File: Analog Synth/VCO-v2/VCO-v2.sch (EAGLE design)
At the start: 64 parts, among them IC1 TL084P, IC2 TL084P, IC3 78L09, IC5 79L09\, Q1 J310, Q2 J310, T1 2N3904, T2 2N3904, T3 2N3904, T4 2N3904, T7 2N3904, U1 CA3096

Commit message: VCO-v2 PWM and Triangle outputs
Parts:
- removed CV_MANUAL: 10k, pot:TRIM_US-B64Y
- removed CV_MANUAL1, CV_MANUAL2: 100k log, pot:TRIM_US-B64Y
- added ATTN_CV_B, ATTN_CV_C: 100k log, pot:TRIM_US-B64Y
- added C10, C9: 100u, rcl:CPOL-USE3.5-10
- added C11, C13, C16, C17: 10u, rcl:CPOL-USE3.5-10
- added C12, C14, C15, C18, C19, C20, C21: 0.1u, resistor:C-EU025-050X050
- added CV-PWM, PWM, TRIANGLE: I/O, !synth_sch:MONO_JACK
- added FREQ-MAN: 10k lin, pot:TRIM_US-B64Y
- added IC7: TL084P, linear:TL084P
- added PWM-MAN: 100k lin, pot:TRIM_US-B64Y
- added R30, R31: 10k, resistor:R-US_0204/7
- added R32, R35, R36: 2.2k, resistor:R-US_0204/7
- added R33, R34, R38: 100k, resistor:R-US_0204/7
- added R37: 47k, resistor:R-US_0204/7
- C8: value 100p -> 0.1u
- IC4: value (none) -> 78L05
- IC6: value (none) -> 79L05
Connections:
- new net N$27: IC2C.-IN, R30.2, R31.2
- new net N$28: R32.1, TRIANGLE.P2
- new net N$36: C21.1
- new net N$37: IC2D.OUT, R35.1
- new net N$38: PWM.P2, R35.2, R36.2
- new net N$39: IC7B.+IN, R37.2
- new net N$40: IC7B.-IN, IC7B.OUT, R34.1
- new net N$41: CV-PWM.P2, R37.1
- new net N$43: IC7A.-IN, R33.2, R34.2, R38.1
- new net N$44: IC2D.-IN, IC7A.OUT, R38.2
- new net N$45: PWM-MAN.S, R33.1
- new net TRIANGLE: IC2C.OUT, IC2D.+IN, R31.1, R32.2
- net +12V: now also C14.1, C8.1, C9.+, IC1P.V+, IC2P.V+
- net +5V: now also C17.+, C19.1, FREQ-MAN.A, PWM-MAN.A; no longer CV_MANUAL.A
- net +9V: now also C11.+, C18.1
- net -12V: now also C10.+, C12.1, C15.1, IC1P.V-, IC2P.V-
- net -5V: now also C16.+, FREQ-MAN.E, PWM-MAN.E; no longer CV_MANUAL.E
- net -9V: now also C13.+, C20.1
- net GND: now also ATTN_CV_B.A, ATTN_CV_C.A, C10.-, C11.-, C12.2, C13.-, C14.2, C15.2, C16.-, C17.-, C18.2, C19.2, C20.2, C21.2, C8.2, C9.-, CV-PWM.P$1, CV-PWM.P3, IC5.GND, IC7A.+IN, PWM.P$1, R30.1, R36.1, TRIANGLE.P$1; no longer CV_MANUAL1.A, CV_MANUAL2.A
- net N$1: now also FREQ-MAN.S; no longer CV_MANUAL.S
- net N$4: now also ATTN_CV_C.S; no longer CV_MANUAL2.S
- net N$6: now also ATTN_CV_B.S; no longer CV_MANUAL1.S
- net N$8: now also ATTN_CV_B.E; no longer CV_MANUAL1.E
- net N$9: now also ATTN_CV_C.E; no longer CV_MANUAL2.E
- net V-CAP-BUFF: now also IC2C.+IN
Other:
- note added: "IC1 power"
- note added: "IC2 power"

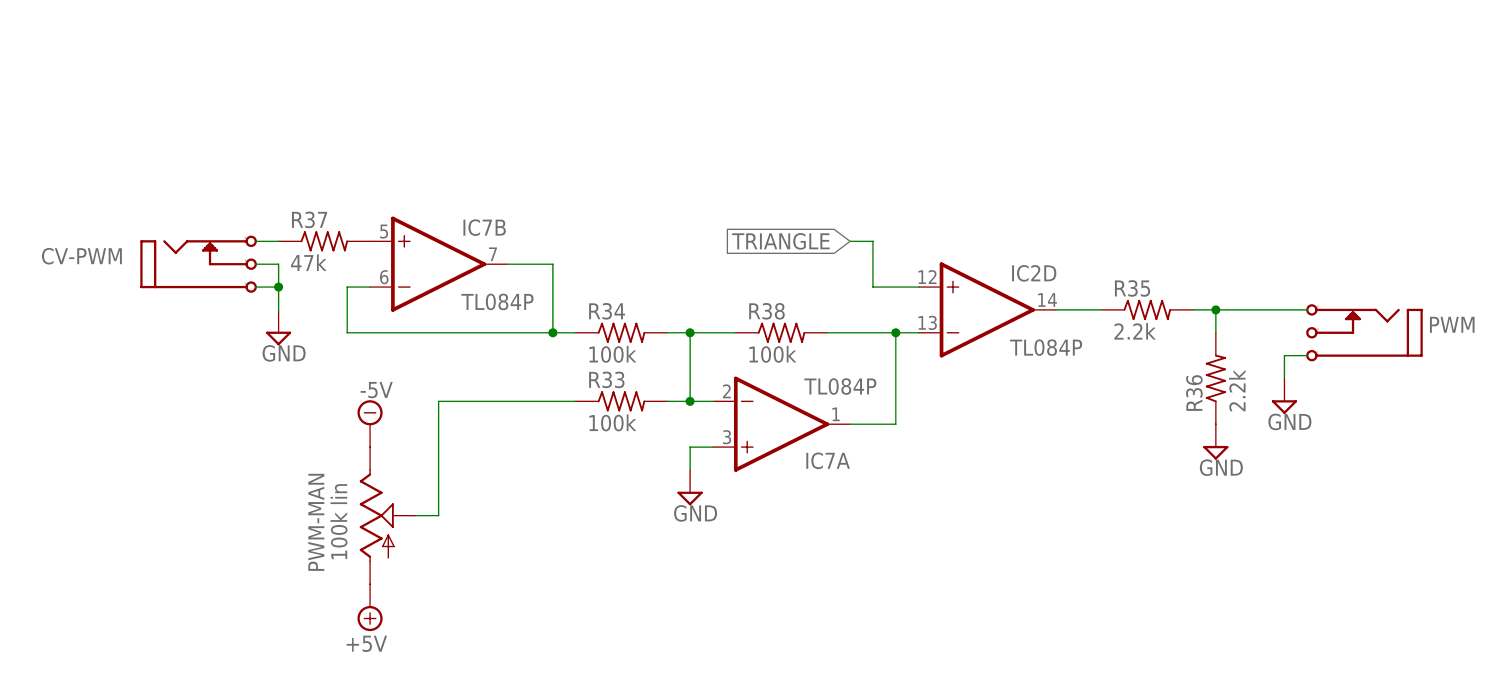
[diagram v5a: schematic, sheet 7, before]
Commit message: VCO-v2 PWM control voltage attenuation
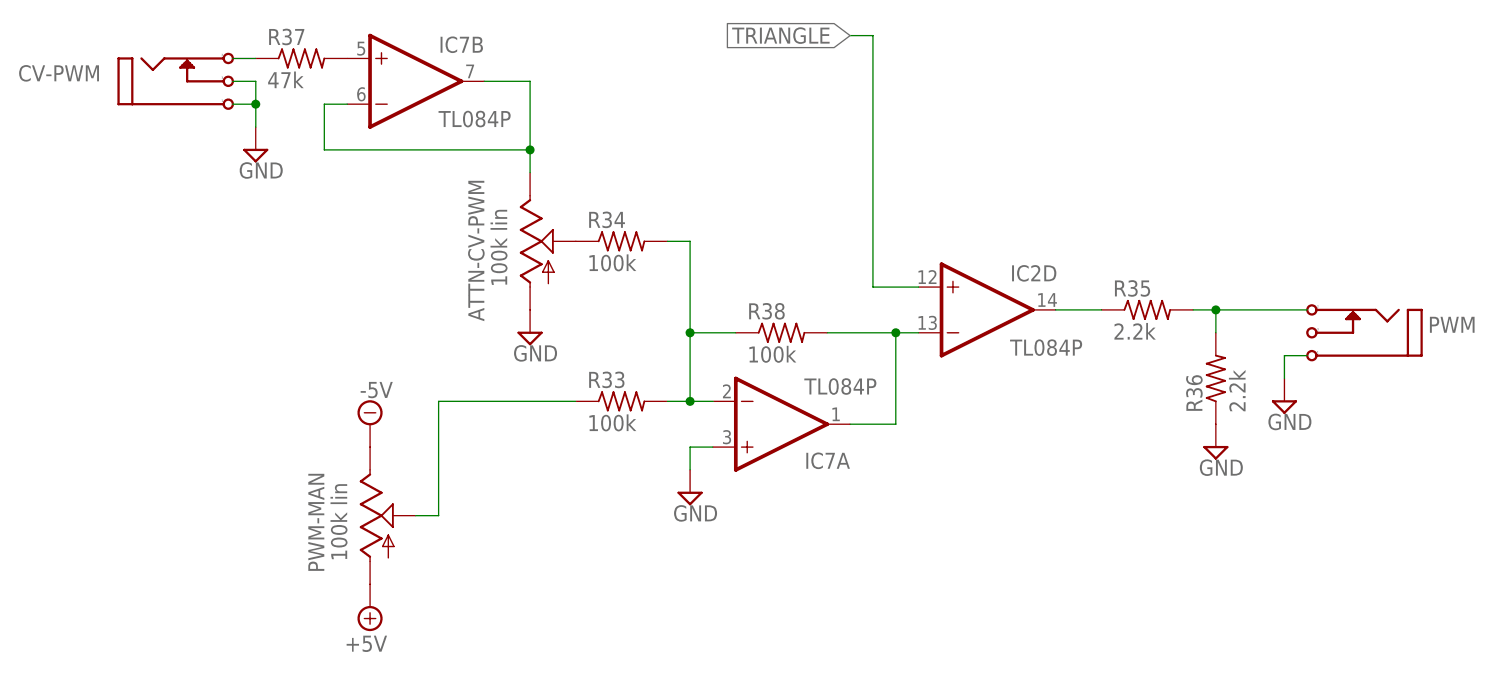
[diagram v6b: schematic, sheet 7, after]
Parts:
- added ATTN-CV-PWM: 100k lin, pot:TRIM_US-B64Y
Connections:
- new net N$42: ATTN-CV-PWM.S, R34.1
- net GND: now also ATTN-CV-PWM.A
- net N$40: now also ATTN-CV-PWM.E; no longer R34.1
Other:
- moved on the sheet: CV-PWM, IC7B, R34, R37
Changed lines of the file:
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@@
 <part name="PWM" library="!synth_sch" deviceset="MONO_JACK" device="" value="I/O"/>
 <part name="SUPPLY36" library="supply2" deviceset="GND" device=""/>
+<part name="ATTN-CV-PWM" library="pot" deviceset="TRIM_US-" device="B64Y" value="100k lin"/>
+<part name="SUPPLY39" library="supply2" deviceset="GND" device=""/>
 </parts>
 <sheets>
@@
 </plain>
 <instances>
-<instance part="IC7" gate="B" x="7.62" y="53.34"/>
+<instance part="IC7" gate="B" x="5.08" y="73.66"/>
 <instance part="IC7" gate="A" x="45.72" y="35.56" rot="MR180"/>
 <instance part="IC2" gate="D" x="68.58" y="48.26"/>
 <instance part="R33" gate="G$1" x="27.94" y="38.1"/>
-<instance part="R34" gate="G$1" x="27.94" y="45.72"/>
+<instance part="R34" gate="G$1" x="27.94" y="55.88"/>
 <instance part="R35" gate="G$1" x="86.36" y="48.26"/>
 <instance part="R36" gate="G$1" x="93.98" y="40.64" rot="R90"/>
 <instance part="SUPPLY40" gate="GND" x="93.98" y="33.02"/>
-<instance part="R37" gate="G$1" x="-5.08" y="55.88"/>
-<instance part="CV-PWM" gate="J1" x="-20.32" y="53.34" smashed="yes">
-<attribute name="NAME" x="-36.576" y="53.34" size="1.778" layer="96"/>
-</instance>
-<instance part="SUPPLY41" gate="GND" x="-10.16" y="45.72"/>
+<instance part="R37" gate="G$1" x="-7.62" y="76.2"/>
+<instance part="CV-PWM" gate="J1" x="-22.86" y="73.66" smashed="yes">
+<attribute name="NAME" x="-39.116" y="73.66" size="1.778" layer="96"/>
+</instance>
+<instance part="SUPPLY41" gate="GND" x="-12.7" y="66.04"/>
 <instance part="R38" gate="G$1" x="45.72" y="45.72"/>
 <instance part="SUPPLY42" gate="+5V" x="0" y="15.24" rot="R180"/>
@@
 </instance>
 <instance part="SUPPLY36" gate="GND" x="101.6" y="38.1"/>
+<instance part="ATTN-CV-PWM" gate="G$1" x="17.78" y="55.88" smashed="yes">
+<attribute name="NAME" x="12.7" y="46.99" size="1.778" layer="95" rot="R90"/>
+<attribute name="VALUE" x="15.24" y="50.8" size="1.778" layer="96" rot="R90"/>
+</instance>
+<instance part="SUPPLY39" gate="GND" x="17.78" y="45.72"/>
 </instances>
 <busses>
@@
 <segment>
 <pinref part="CV-PWM" gate="J1" pin="P3"/>
-<wire x1="-12.7" y1="53.34" x2="-10.16" y2="53.34" width="0.1524" layer="91"/>
-<wire x1="-10.16" y1="53.34" x2="-10.16" y2="50.8" width="0.1524" layer="91"/>
+<wire x1="-15.24" y1="73.66" x2="-12.7" y2="73.66" width="0.1524" layer="91"/>
+<wire x1="-12.7" y1="73.66" x2="-12.7" y2="71.12" width="0.1524" layer="91"/>
 <pinref part="CV-PWM" gate="J1" pin="P$1"/>
-<wire x1="-10.16" y1="50.8" x2="-12.7" y2="50.8" width="0.1524" layer="91"/>
-<wire x1="-10.16" y1="50.8" x2="-10.16" y2="48.26" width="0.1524" layer="91"/>
-<junction x="-10.16" y="50.8"/>
+<wire x1="-12.7" y1="71.12" x2="-15.24" y2="71.12" width="0.1524" layer="91"/>
+<wire x1="-12.7" y1="71.12" x2="-12.7" y2="68.58" width="0.1524" layer="91"/>
+<junction x="-12.7" y="71.12"/>
 <pinref part="SUPPLY41" gate="GND" pin="GND"/>
 </segment>
@@
 <wire x1="101.6" y1="43.18" x2="104.14" y2="43.18" width="0.1524" layer="91"/>
 </segment>
+<segment>
+<pinref part="ATTN-CV-PWM" gate="G$1" pin="A"/>
+<pinref part="SUPPLY39" gate="GND" pin="GND"/>
+</segment>
 </net>
 <net name="TRIANGLE" class="0">
@@
 <pinref part="IC2" gate="D" pin="+IN"/>
 <wire x1="60.96" y1="50.8" x2="55.88" y2="50.8" width="0.1524" layer="91"/>
-<wire x1="55.88" y1="50.8" x2="55.88" y2="55.88" width="0.1524" layer="91"/>
-<wire x1="55.88" y1="55.88" x2="53.34" y2="55.88" width="0.1524" layer="91"/>
-<label x="53.34" y="55.88" size="1.778" layer="95" rot="R180" xref="yes"/>
+<wire x1="55.88" y1="50.8" x2="55.88" y2="78.74" width="0.1524" layer="91"/>
+<wire x1="55.88" y1="78.74" x2="53.34" y2="78.74" width="0.1524" layer="91"/>
+<label x="53.34" y="78.74" size="1.778" layer="95" rot="R180" xref="yes"/>
 </segment>
 </net>
@@
 <segment>
 <pinref part="IC7" gate="B" pin="-IN"/>
-<wire x1="0" y1="50.8" x2="-2.54" y2="50.8" width="0.1524" layer="91"/>
-<wire x1="-2.54" y1="50.8" x2="-2.54" y2="45.72" width="0.1524" layer="91"/>
-<wire x1="-2.54" y1="45.72" x2="20.32" y2="45.72" width="0.1524" layer="91"/>
-<wire x1="20.32" y1="45.72" x2="20.32" y2="53.34" width="0.1524" layer="91"/>
+<wire x1="-2.54" y1="71.12" x2="-5.08" y2="71.12" width="0.1524" layer="91"/>
+<wire x1="-5.08" y1="71.12" x2="-5.08" y2="66.04" width="0.1524" layer="91"/>
+<wire x1="-5.08" y1="66.04" x2="17.78" y2="66.04" width="0.1524" layer="91"/>
+<wire x1="17.78" y1="66.04" x2="17.78" y2="73.66" width="0.1524" layer="91"/>
 <pinref part="IC7" gate="B" pin="OUT"/>
-<wire x1="20.32" y1="53.34" x2="15.24" y2="53.34" width="0.1524" layer="91"/>
-<pinref part="R34" gate="G$1" pin="1"/>
-<wire x1="22.86" y1="45.72" x2="20.32" y2="45.72" width="0.1524" layer="91"/>
-<junction x="20.32" y="45.72"/>
+<wire x1="17.78" y1="73.66" x2="12.7" y2="73.66" width="0.1524" layer="91"/>
+<pinref part="ATTN-CV-PWM" gate="G$1" pin="E"/>
+<wire x1="17.78" y1="63.5" x2="17.78" y2="66.04" width="0.1524" layer="91"/>
+<junction x="17.78" y="66.04"/>
 </segment>
 </net>
@@
 <segment>
 <pinref part="R37" gate="G$1" pin="1"/>
-<wire x1="-10.16" y1="55.88" x2="-12.7" y2="55.88" width="0.1524" layer="91"/>
+<wire x1="-12.7" y1="76.2" x2="-15.24" y2="76.2" width="0.1524" layer="91"/>
 <pinref part="CV-PWM" gate="J1" pin="P2"/>
 </segment>
@@
 <wire x1="35.56" y1="38.1" x2="35.56" y2="45.72" width="0.1524" layer="91"/>
 <pinref part="R34" gate="G$1" pin="2"/>
-<wire x1="33.02" y1="45.72" x2="35.56" y2="45.72" width="0.1524" layer="91"/>
+<wire x1="33.02" y1="55.88" x2="35.56" y2="55.88" width="0.1524" layer="91"/>
+<wire x1="35.56" y1="55.88" x2="35.56" y2="45.72" width="0.1524" layer="91"/>
 <junction x="35.56" y="45.72"/>
 <pinref part="IC7" gate="A" pin="-IN"/>
@@
 </segment>
 </net>
+<net name="N$42" class="0">
+<segment>
+<pinref part="R34" gate="G$1" pin="1"/>
+<pinref part="ATTN-CV-PWM" gate="G$1" pin="S"/>
+</segment>
+</net>

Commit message: VCO-v2 Sine (from VCO-v1 basically)
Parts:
- added Q3, Q4: 2N3904, transistor-npn:2N3904
- added R-SINE-AMPL, R-SINE-ROUND: 100k lin, pot:TRIM_US-B64Y
- added R-SINE-SYMM: 10 kΩ, pot:TRIM_US-B64Y
- added R39, R40: 2.2 kΩ, resistor:R-US_0204/7
- added R41: 390 Ω, resistor:R-US_0204/7
- added R42: 18 kΩ, resistor:R-US_0204/7
- added R43, R44, R45, R46: 10 kΩ, resistor:R-US_0204/7
- added R47: 1k, resistor:R-US_0204/7
- added SINE: I/O, !synth_sch:MONO_JACK
- R32: value 2.2k -> 1k
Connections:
- net N$37 renamed PWM
- new net N$37: Q3.B, R-SINE-ROUND.E, R39.1
- new net N$46: Q4.B, R40.1
- new net N$47: Q3.E, R-SINE-SYMM.A, R41.1
- new net N$48: Q4.E, R-SINE-SYMM.E, R41.2
- new net N$49: R-SINE-SYMM.S, R42.1
- new net N$50: IC7C.-IN, Q3.C, R43.1, R46.1
- new net N$51: IC7C.OUT, R-SINE-AMPL.A, R46.2
- new net N$52: IC7C.+IN, Q4.C, R44.1, R45.2
- new net N$54: IC7D.-IN, R-SINE-AMPL.S
- new net N$55: R47.2, SINE.P2
- new net SINE: IC7D.OUT, R-SINE-AMPL.E, R47.1
- net +9V: now also R43.2, R44.2
- net -9V: now also R42.2
- net GND: now also IC7D.+IN, R39.2, R40.2, R45.1, SINE.P$1
- net TRIANGLE: now also R-SINE-ROUND.A, R-SINE-ROUND.S
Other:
- note added: "Triangle to Sine converter is a modified version of Thomas Henry's design."

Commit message: VCO-v2 LEDs sheet and signal names
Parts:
- added LED-CV-A, LED-CV-B, LED-CV-PWM, LED-PWM, LED-SINE, LED-TRIANGLE, LED_CV-C: (no value), led:LED3MM
- added R48, R49, R50, R51, R53, R54, R56: 4.7 kΩ, resistor:R-US_0204/7
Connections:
- removed net N$11: IC1C.-IN, IC1C.OUT, R6.1
- removed net N$5: IC1B.-IN, IC1B.OUT, R5.1
- removed net N$7: IC1A.-IN, IC1A.OUT, R4.1
- new net CV-A: IC1A.-IN, IC1A.OUT, LED-CV-A.A, R4.1
- new net CV-B: IC1B.-IN, IC1B.OUT, LED-CV-B.A, R5.1
- new net CV-C: IC1C.-IN, IC1C.OUT, LED_CV-C.A, R6.1
- new net CV-PWM: IC2D.-IN, IC7A.OUT, LED-CV-PWM.C, R38.2
- new net N$53: LED-CV-A.C, R48.1
- new net N$56: LED-CV-B.C, R49.1
- new net N$57: LED_CV-C.C, R50.1
- new net N$59: LED-PWM.C, R53.1
- new net N$60: LED-TRIANGLE.C, R56.1
- new net N$61: LED-SINE.C, R54.1
- net -5V: now also R48.2, R49.2, R50.2, R51.2, R53.2, R54.2, R56.2
- net N$3: now also IC1B.+IN, IC1C.+IN
- net N$44: now also LED-CV-PWM.A, R51.1; no longer IC2D.-IN, IC7A.OUT, R38.2
- net PWM: now also LED-PWM.A
- net SINE: now also LED-SINE.A
- net TRIANGLE: now also LED-TRIANGLE.A
